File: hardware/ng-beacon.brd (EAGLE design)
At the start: 71.1 x 76.2 mm, 5 parts

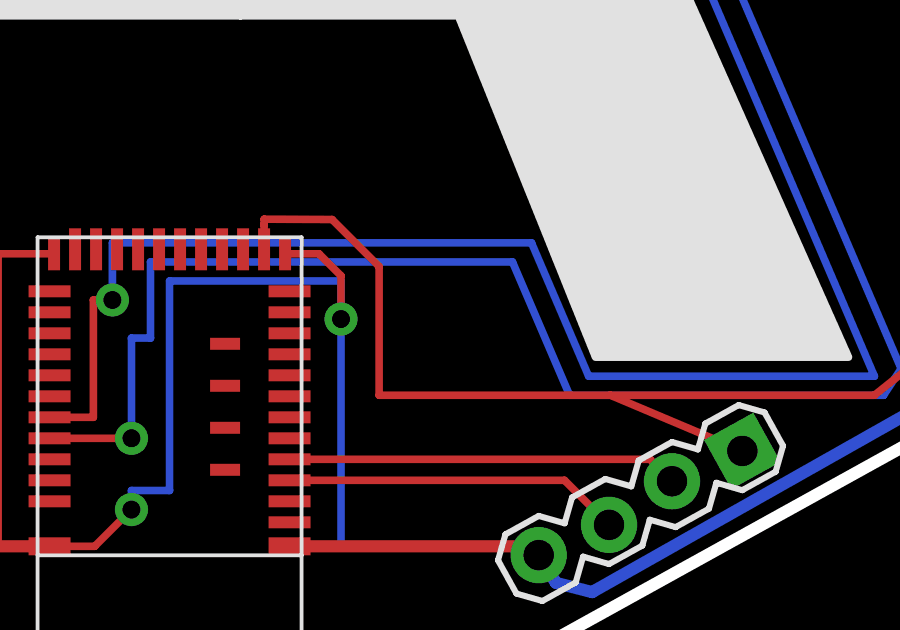
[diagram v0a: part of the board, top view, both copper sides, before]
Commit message: add reset pads (sort of)
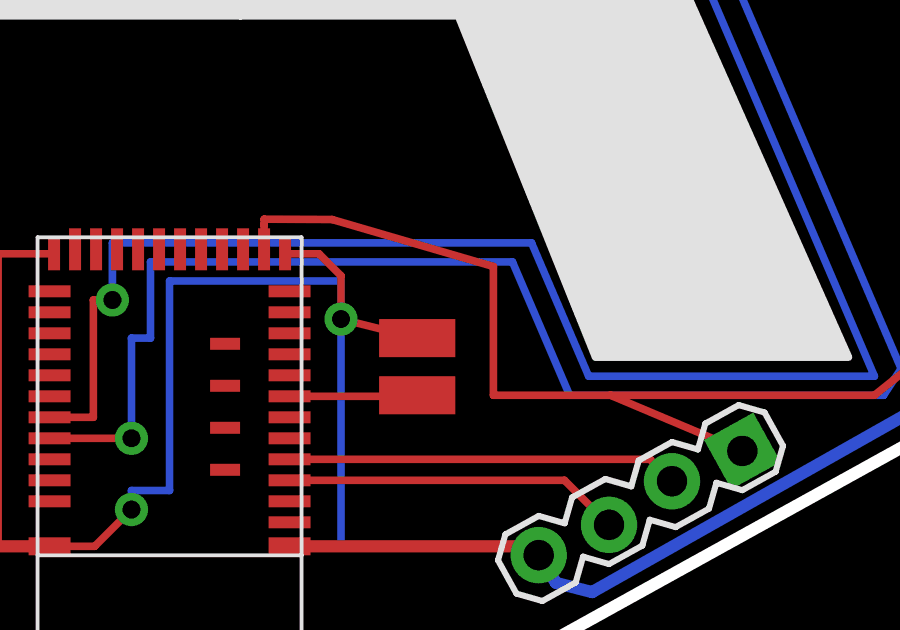
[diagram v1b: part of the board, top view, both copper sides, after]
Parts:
- added PAD1, PAD2: (no value), wirepad:SMD1,27-2,54
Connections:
- new net N$4: PAD1.1, U$2.8
- net GND: now also PAD2.1
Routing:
- net N$4: track 0.00 -> 4.26 mm
- net GND: track 166.8 -> 169.4 mm
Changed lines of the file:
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@@
 <layer number="220" name="220bmp" color="21" fill="1" visible="no" active="no"/>
 <layer number="221" name="221bmp" color="22" fill="1" visible="no" active="no"/>
+<layer number="222" name="222bmp" color="23" fill="1" visible="no" active="no"/>
 <layer number="223" name="223bmp" color="24" fill="1" visible="no" active="no"/>
 <layer number="224" name="224bmp" color="25" fill="1" visible="no" active="no"/>
@@
 <attribute name="VALUE" x="44.63" y="17.735" size="0.8128" layer="27" font="vector" ratio="5" rot="R270"/>
 </element>
+<element name="PAD1" library="wirepad" package="SMD1,27-2,54" value="" x="53.975" y="13.97" smashed="yes" rot="R90">
+<attribute name="VALUE" x="53.975" y="13.97" size="0.0254" layer="27" rot="R90"/>
+</element>
+<element name="PAD2" library="wirepad" package="SMD1,27-2,54" value="" x="53.975" y="15.875" smashed="yes" rot="R90">
+<attribute name="VALUE" x="53.975" y="15.875" size="0.0254" layer="27" rot="R90"/>
+</element>
 </elements>
 <signals>
@@
 <wire x1="41.87" y1="18.685" x2="40.005" y2="18.685" width="0.254" layer="1"/>
 <wire x1="40.005" y1="18.685" x2="40.005" y2="8.935" width="0.254" layer="1"/>
+<contactref element="PAD2" pad="1"/>
+<wire x1="53.975" y1="15.875" x2="51.435" y2="16.51" width="0.254" layer="1"/>
 </signal>
 <signal name="N$1">
@@
 <wire x1="71.12" y1="38.1" x2="75.064034375" y2="38.080853125" width="0.254" layer="1"/>
 <contactref element="U$2" pad="15"/>
-<wire x1="60.41543125" y1="13.97" x2="52.705" y2="13.97" width="0.254" layer="1"/>
-<wire x1="52.705" y1="13.97" x2="52.705" y2="18.260925" width="0.254" layer="1"/>
-<wire x1="52.705" y1="18.260925" x2="51.13753125" y2="19.82839375" width="0.254" layer="1"/>
+<wire x1="60.41543125" y1="13.97" x2="56.515" y2="13.97" width="0.254" layer="1"/>
+<wire x1="56.515" y1="13.97" x2="56.515" y2="18.260925" width="0.254" layer="1"/>
+<wire x1="56.515" y1="18.260925" x2="51.13753125" y2="19.82839375" width="0.254" layer="1"/>
 <wire x1="51.13753125" y1="19.82839375" x2="48.8734625" y2="19.83935625" width="0.254" layer="1"/>
 <wire x1="48.8734625" y1="19.83935625" x2="48.87016875" y2="19.668740625" width="0.254" layer="1"/>
@@
 <signal name="N$2">
 </signal>
+<signal name="N$4">
+<contactref element="U$2" pad="8"/>
+<contactref element="PAD1" pad="1"/>
+<wire x1="49.72" y1="13.935" x2="53.34" y2="13.935" width="0.254" layer="1"/>
+<wire x1="53.34" y1="13.935" x2="53.975" y2="13.97" width="0.254" layer="1"/>
+</signal>
 </signals>
